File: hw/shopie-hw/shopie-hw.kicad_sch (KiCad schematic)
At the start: 29 parts, among them J1 Jack-DC, SW1 SW_SPDT, SW2 SW_MEC_5E, SW3 SW_SPDT, U2 STM32F405RGT6, U3 LM2596T-5, U4 AP2112K-3.3

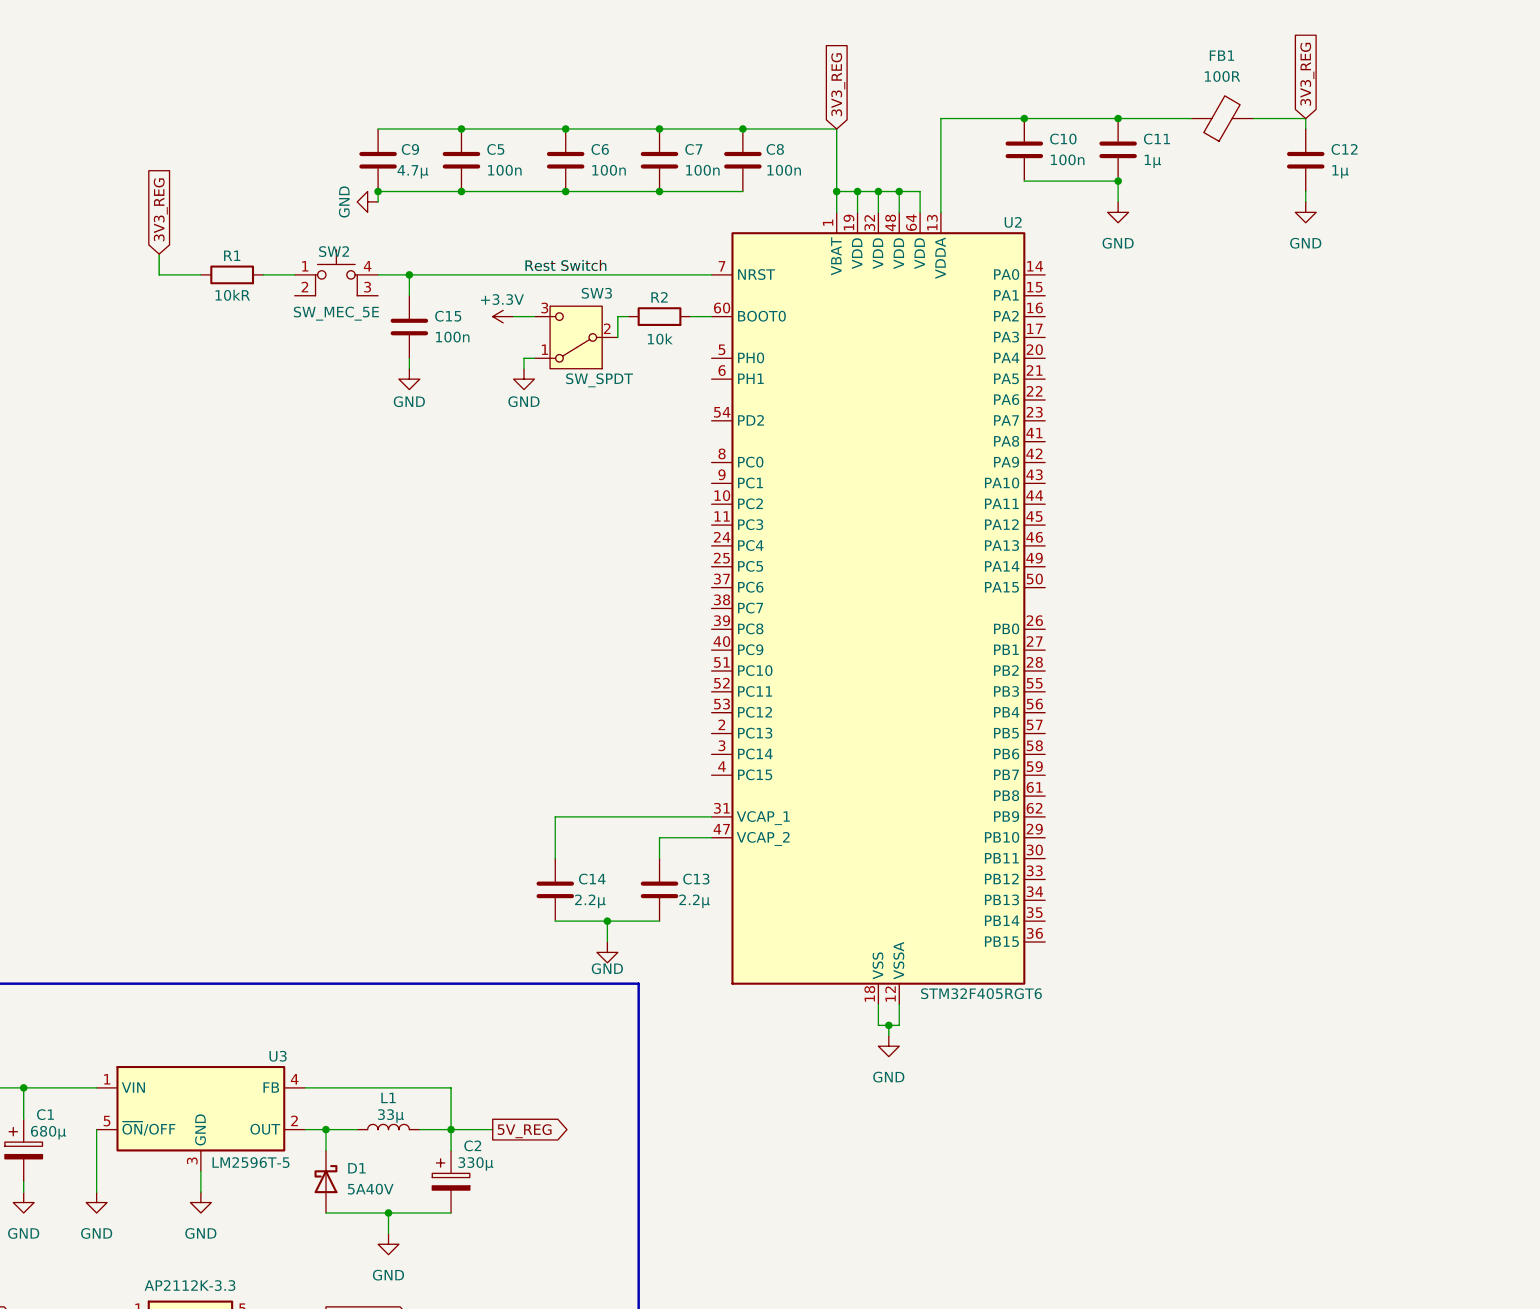
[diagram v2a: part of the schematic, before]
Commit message: Add external 8MHz crystal oscillator circuit
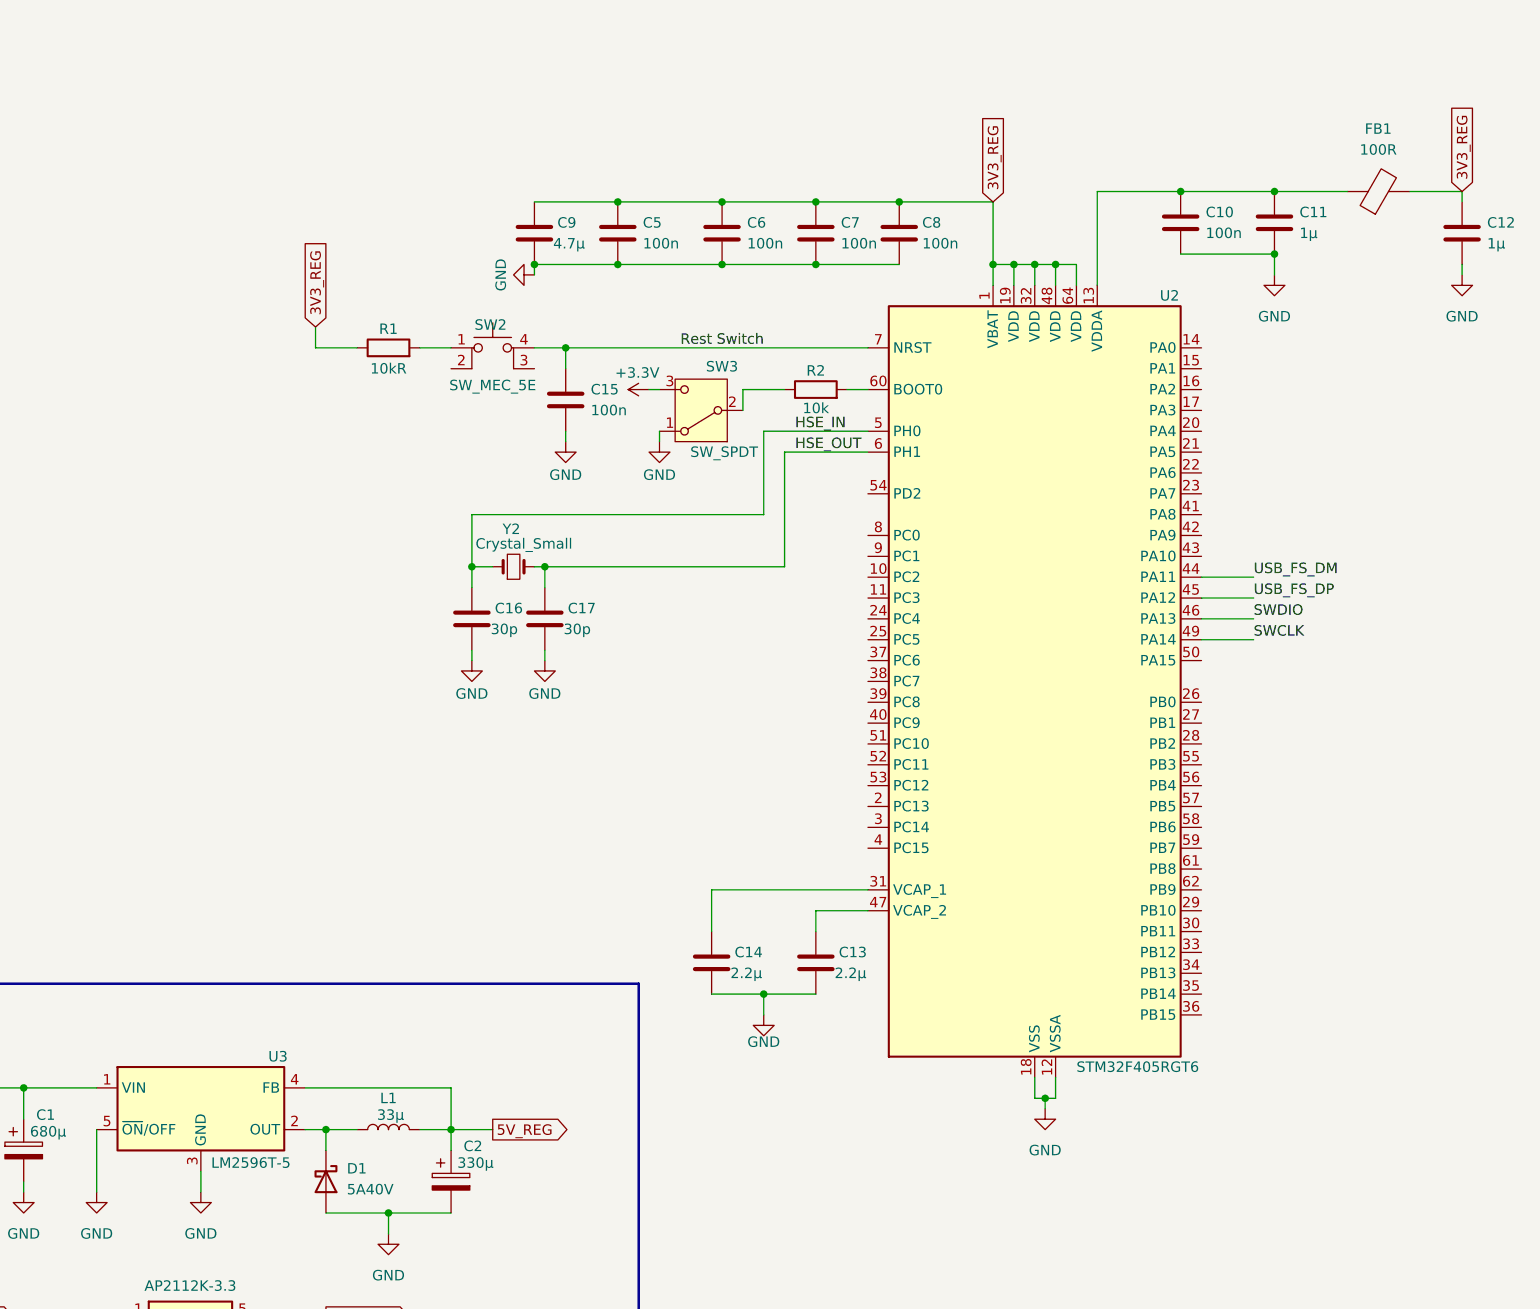
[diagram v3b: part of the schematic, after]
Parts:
- added C16, C17: 30p, symbol Device:C
- added Y2: Crystal_Small, symbol Device:Crystal_Small
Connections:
- net GND: now also C16.2, C17.2
- net USB_FS_DM: now reaches U2.44 (PA11)
- net USB_FS_DP: now reaches U2.45 (PA12)
- net SWDIO: now reaches U2.46 (PA13)
- net SWCLK: now reaches U2.49 (PA14)
- net HSE_IN: now reaches U2.5 (PH0)
- net HSE_IN: now also C16.1, Y2.1
- net HSE_OUT: now reaches U2.6 (PH1)
- net HSE_OUT: now also C17.1, Y2.2
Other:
- moved on the sheet: C10, C11, C12, C13, C14, C15, C5, C6, C7, C8, C9, FB1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

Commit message: Add USB connector and SWD debug header, update power switch circuit with 5V option
- Added USB-Micro connectro symbol and routed D+, D- and VBUS
- Connected 1k5 pull up resistor to D+ for usb device detection
- Connected SWDIO and SWCLK to debug headers
- Modified power switch circuit to support both battery (14V8) and USB (5V) as input.
- Renamed some shared power nets accordingly.
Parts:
- added J2: USB_B_Micro, symbol Connector:USB_B_Micro
- added J3: Conn_01x04_Socket, symbol Connector:Conn_01x04_Socket
- added R3: 1k5, symbol Device:R
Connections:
- net 3V3_REG is gone; now on net +3.3V: C12.1, C4.1, C5.1, C6.1, C7.1, C8.1, C9.1, FB1.2, R1.1, U2.1 (VBAT), U2.19 (VDD), U2.32 (VDD), U2.48 (VDD), U2.64 (VDD), U4.5 (VOUT)
- net +3.3V: now also J3.1 (Pin_1), R3.2
- net GND: now also J2.5 (GND), J3.4 (Pin_4)
- net SWCLK: now also J3.3 (Pin_3)
- net SWDIO: now also J3.2 (Pin_2)
- net USB_FS_DM: now also J2.2 (D-)
- net USB_FS_DP: now also J2.3 (D+), R3.1
- net VBUS: now reaches SW1.1 (A)
- net VBUS: now also J2.1 (VBUS)
- net 14V8 renamed V_USB_BAT
- net 5V_REG renamed +5V
- no-connect marks 1 -> 2

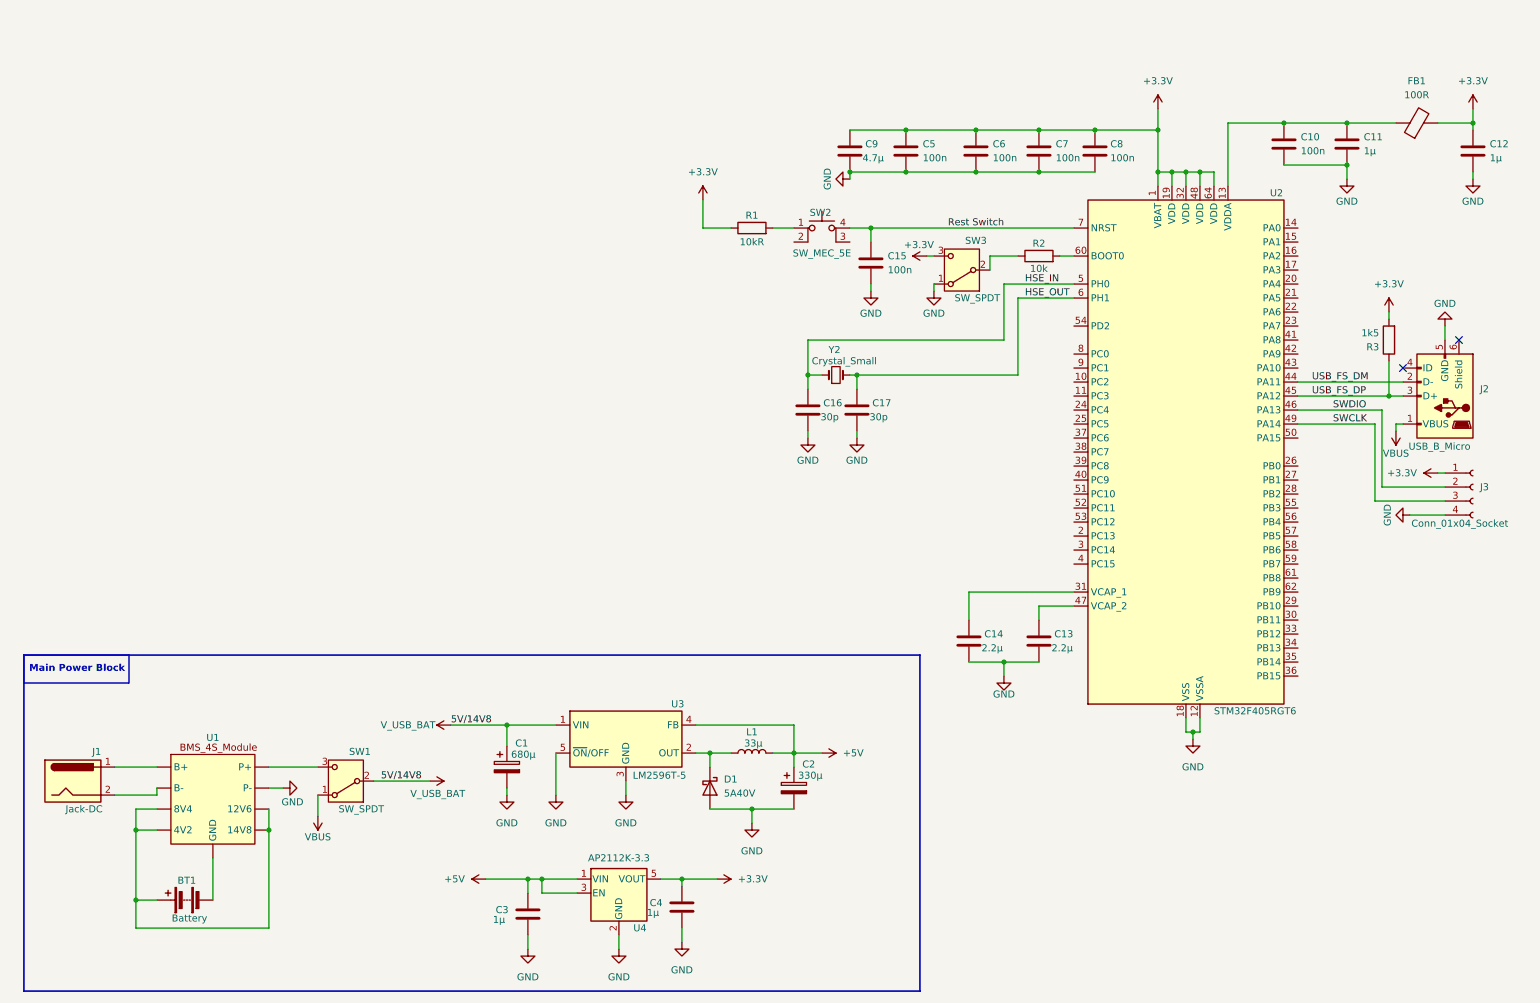
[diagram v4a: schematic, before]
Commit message: Finalized Power and MCU Schematic Page
- Added a LED indictor when MCU is powered
- Added textual labels to clarify sections of the schematic
- Assigned page title to the schematic sheet
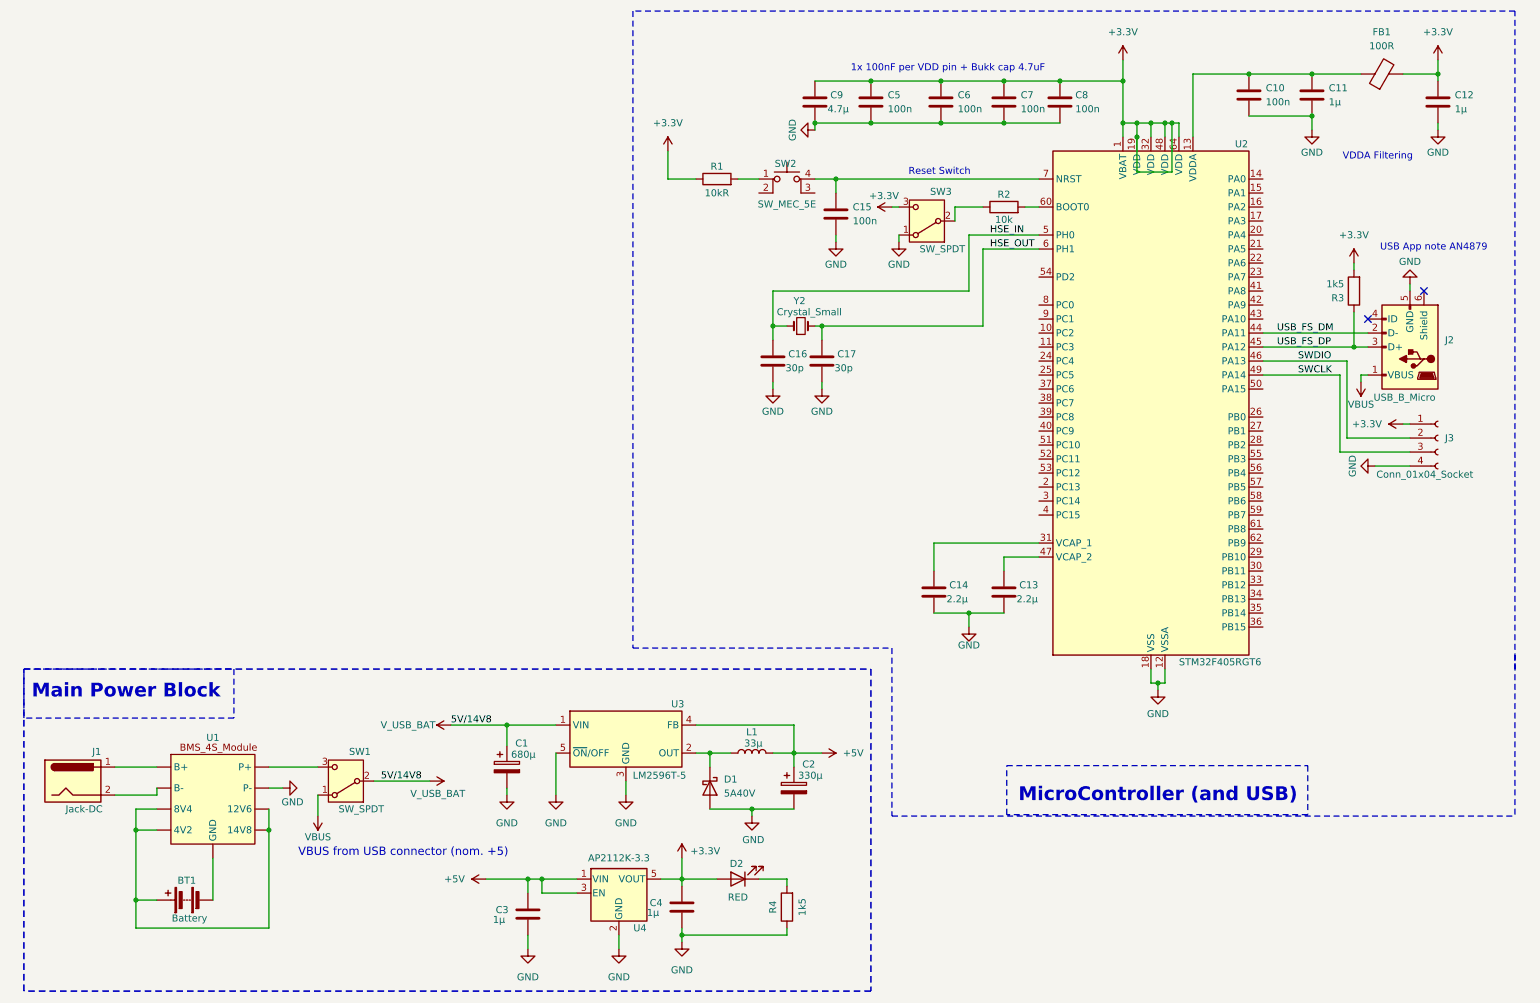
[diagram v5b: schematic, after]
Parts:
- added D2: RED, symbol Device:LED
- added R4: 1k5, symbol Device:R
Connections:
- net +3.3V: now also D2.2 (A)
- net GND: now also R4.1
- net Rest Switch: no longer names the net of C15.1, SW2.4 (A), U2.7 (NRST)
- new net: D2.1 (K), R4.2
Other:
- note added: "1x 100nF per VDD pin + Bukk cap 4.7uF"
- note added: "MicroController (and USB)"
- note added: "Reset Switch"
- note added: "USB App note AN4879"
- note added: "VBUS from USB connector (nom. +5)"
- note added: "VDDA Filtering"
- company: (none) -> Shopie-hw
- title: (none) -> Power and MCU Core 
- moved on the sheet: C10, C11, C12, C13, C14, C15, C16, C17, C5, C6, C7, C8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
